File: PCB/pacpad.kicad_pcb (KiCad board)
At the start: 2 copper layers, 68 x 65 mm, 9 parts, among them SW1 SW_Push, SW2 SW_Push, SW3 SW_Push, SW4 SW_Push, SW5 RotaryEncoder_Switch, U1 MOUDLE-SEEEDUINO-XIAO, U2 ER_OLEDM0.91_1x-I2C

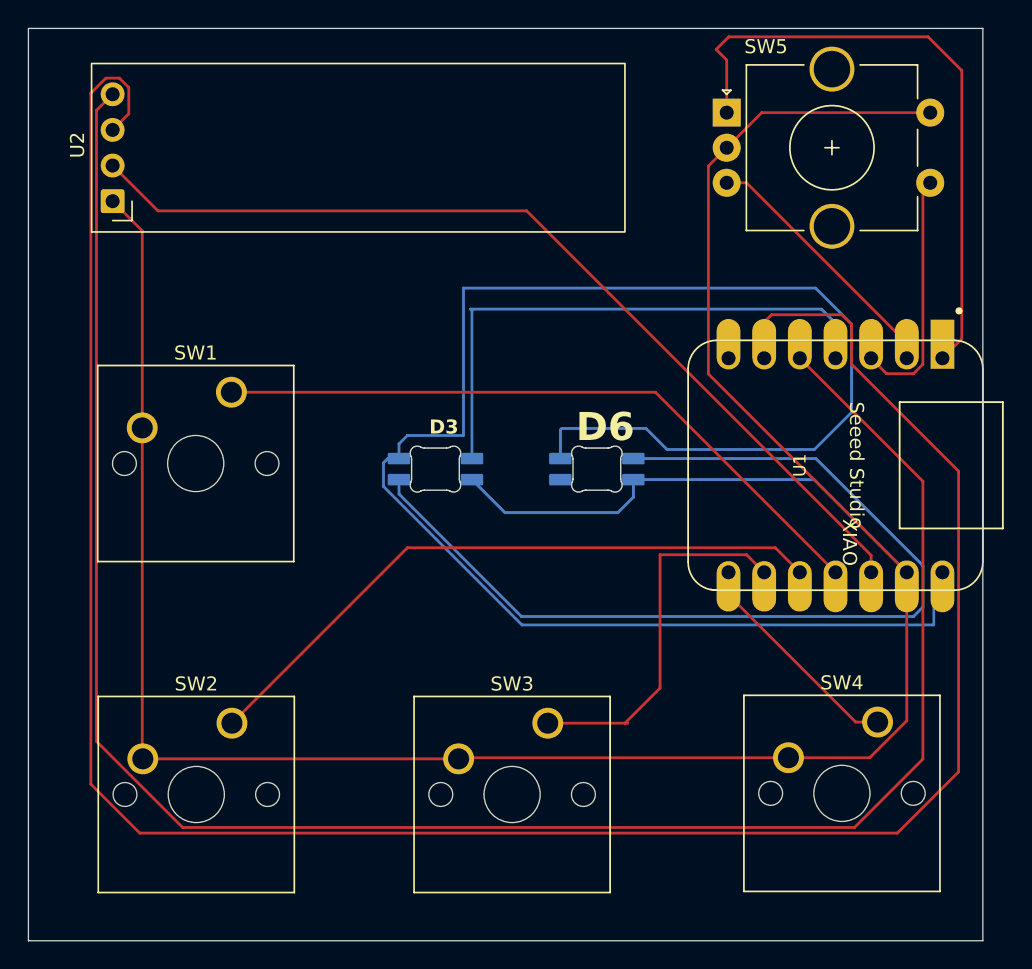
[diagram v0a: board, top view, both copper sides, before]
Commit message: Added everything except the firmkware
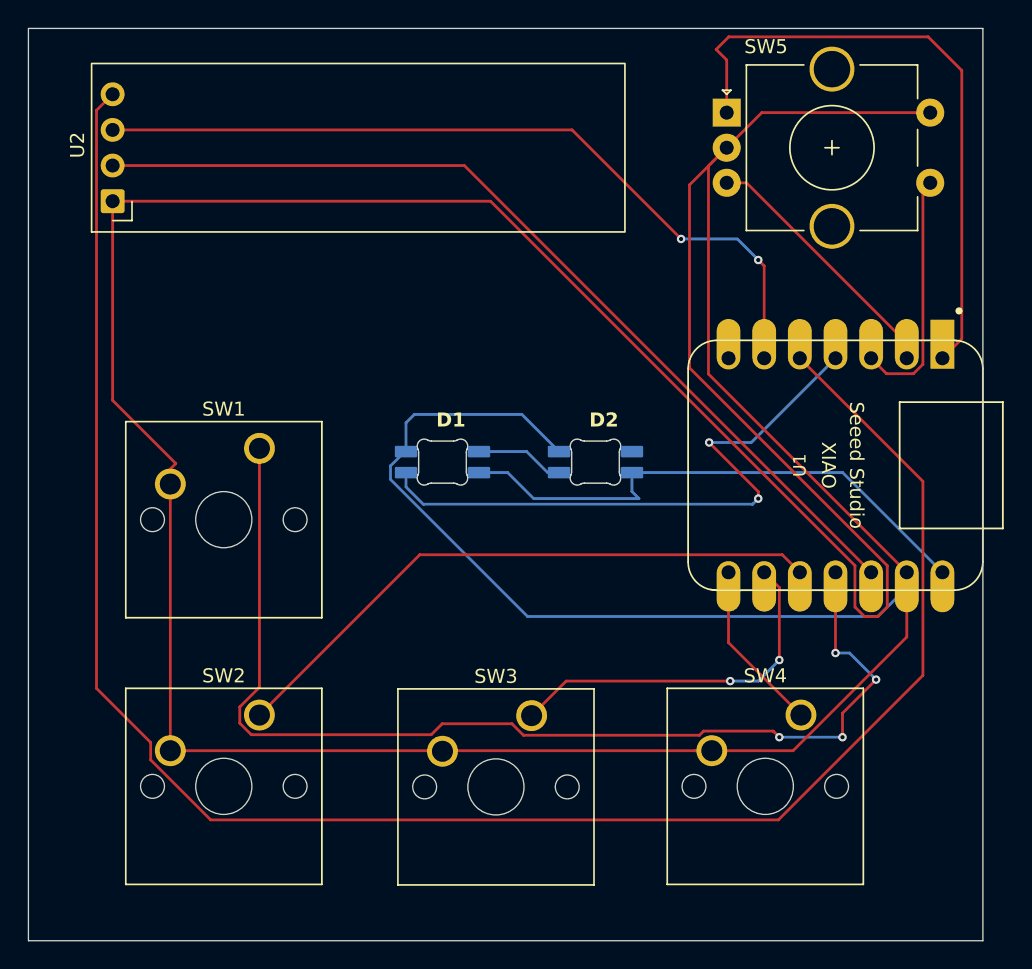
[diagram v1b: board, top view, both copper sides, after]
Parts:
- removed D3: #1, pacpadig:SK6812MINI-E_fixed
- removed D6: #2, pacpadig:SK6812MINI-E_fixed
- added D1: SK6812MINI-E, pacpad_F:SK6812MINI-E_fixed, F.Cu at (133.5, 57.5)
- added D2: SK6812MINI-E, pacpad_F:SK6812MINI-E_fixed, F.Cu at (144.4, 57.5)
- U1: footprint pacpadig:XIAO-Generic-Hybrid-14P-2.54-21X17.8MM -> pacpad_F:XIAO-Generic-Hybrid-14P-2.54-21X17.8MM
- moved SW4 5.48 mm to (159.0, 75.4)
- moved SW1 4.47 mm to (120.5, 56.4)
- moved SW2 2.04 mm to (120.5, 75.4)
- moved SW3 1.27 mm to (139.8, 75.5)
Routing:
- net GND: track 195.9 -> 324.2 mm
- net Net-(U1-PA9_A5_D5_SCL): track 165.6 -> 57.0 mm, vias 0 -> 2
- net Net-(D1-VDD): track 127.2 -> 41.3 mm
- net Net-(D3-DOUT): track 69.0 -> 0.00 mm
- net Net-(U1-PA6_A10_D10_MOSI): track 48.4 -> 78.9 mm, vias 0 -> 4
- net Net-(D1-DIN): track 39.6 -> 46.2 mm, vias 0 -> 3
- net Net-(D1-DOUT): track 0.00 -> 6.32 mm
- net Net-(U1-PA8_A4_D4_SDA): track 142.2 -> 136.8 mm
- net Net-(U1-PB09_A7_D7_RX): track 16.0 -> 12.3 mm
- net Net-(U1-PA5_A9_D9_MISO): track 46.4 -> 43.7 mm
- net Net-(U1-3V3): track 66.8 -> 66.0 mm
- net Net-(U1-PA7_A8_D8_SCK): track 27.7 -> 27.0 mm, vias 0 -> 2

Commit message: Added gerbers in production
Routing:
- net Net-(D1-DIN): vias 3 -> 2
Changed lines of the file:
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@@
-		(net "Net-(D1-DIN)")
-	)
-	(via
-		(at 161.5 50)
-		(size 0.6)
-		(drill 0.3)
-		(layers "F.Cu" "B.Cu")
 		(net "Net-(D1-DIN)")
 	)

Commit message: Update: PCB with gerbers.zip
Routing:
- net GND: track 324.2 -> 188.7 mm
- net Net-(U1-PA8_A4_D4_SDA): track 136.8 -> 64.8 mm
- net Net-(U1-PA6_A10_D10_MOSI): track 78.9 -> 48.2 mm, vias 4 -> 0
- net Net-(U1-PA4_A1_D1): track 18.6 -> 33.5 mm
- net Net-(U1-PA02_A0_D0): track 44.7 -> 35.4 mm
- net Net-(U1-PB09_A7_D7_RX): track 12.3 -> 19.7 mm, vias 0 -> 2
- net Net-(U1-3V3): track 66.0 -> 72.6 mm
- net Net-(U1-PA5_A9_D9_MISO): track 43.7 -> 50.1 mm
- net Net-(U1-PA7_A8_D8_SCK): track 27.0 -> 21.4 mm, vias 2 -> 0
- net Net-(D1-DIN): track 46.2 -> 41.3 mm
- net Net-(U1-PA9_A5_D5_SCL): track 57.0 -> 60.7 mm, vias 2 -> 0
- net Net-(U1-PA10_A2_D2): track 17.6 -> 14.2 mm
- net Net-(D1-VDD): track 41.3 -> 42.6 mm
